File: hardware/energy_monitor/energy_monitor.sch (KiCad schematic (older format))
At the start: 134 parts, among them J1 Screw_Terminal_01x03, J2 Screw_Terminal_01x04, J3 Screw_Terminal_01x04, J4 Screw_Terminal_01x04, J5 USB_OTG, Q1 MMBT2222, Q2 MMBT2222, U1 RAC04, U2 TPS730, U3 TPS723, U4 ADS131E08, U5 AP2112, U6 CP2104, U7 ESP-WROOM-32U

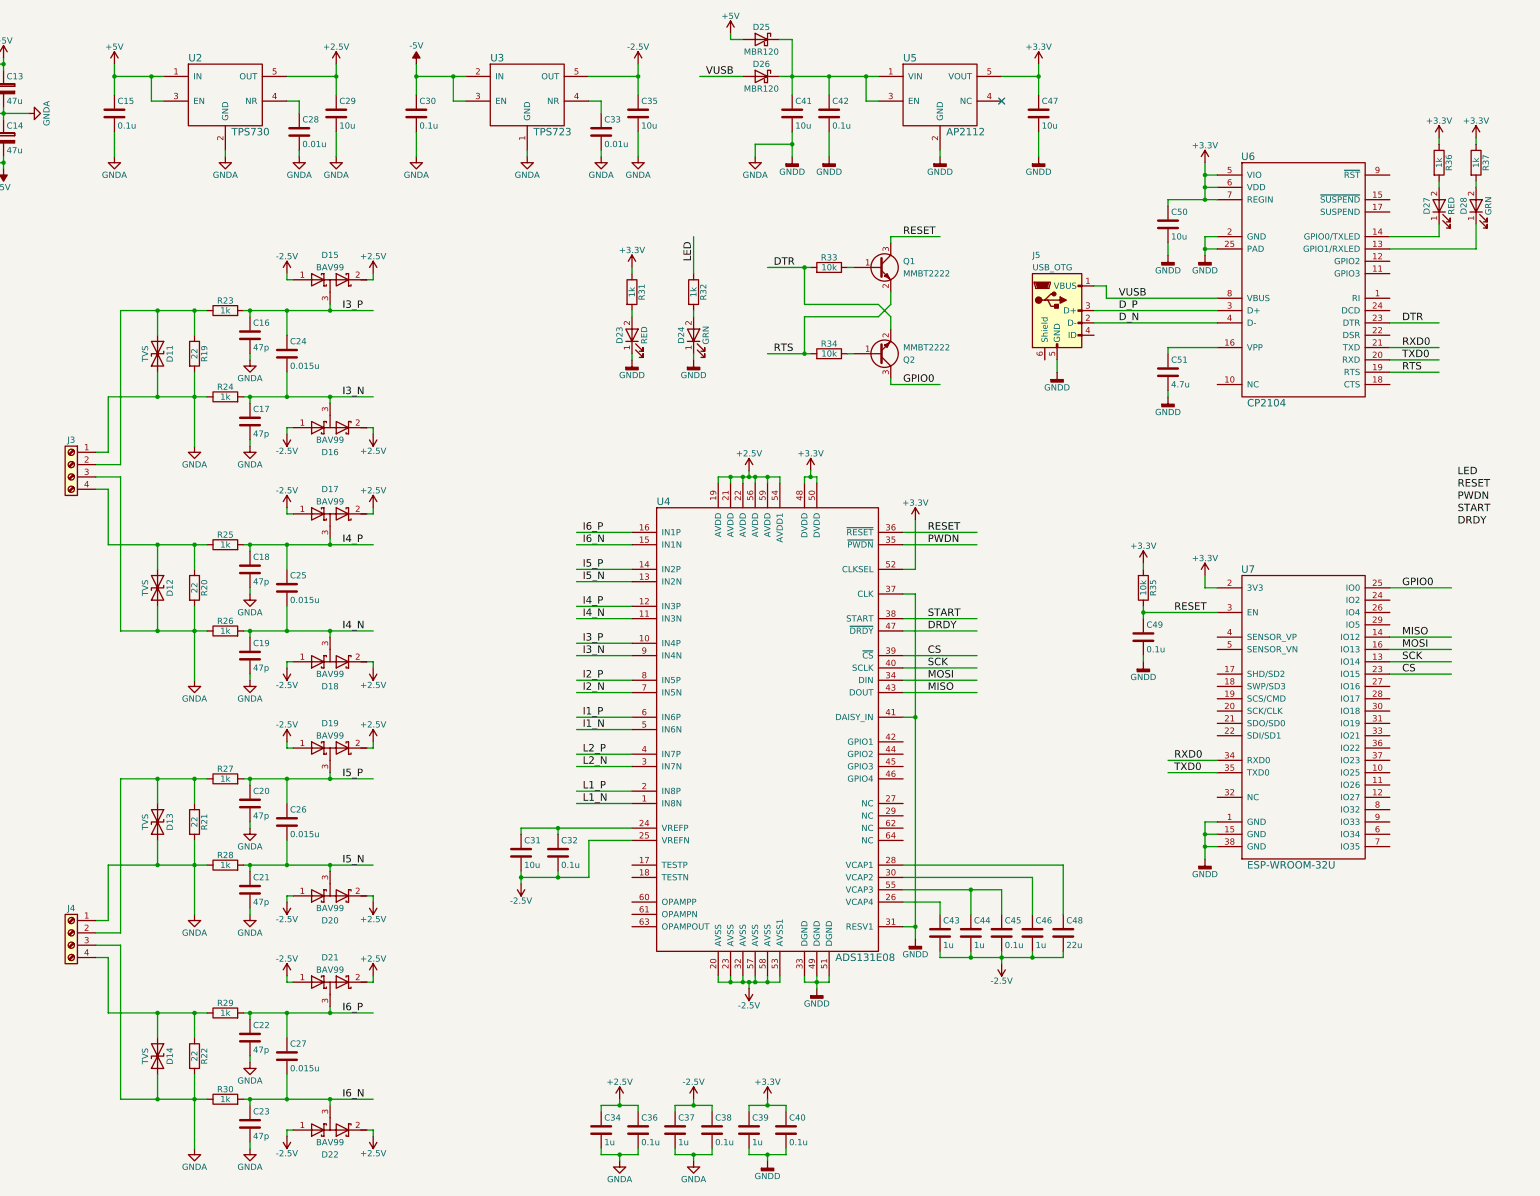
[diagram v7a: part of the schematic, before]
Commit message: Added digital isolator to USB UART circuit
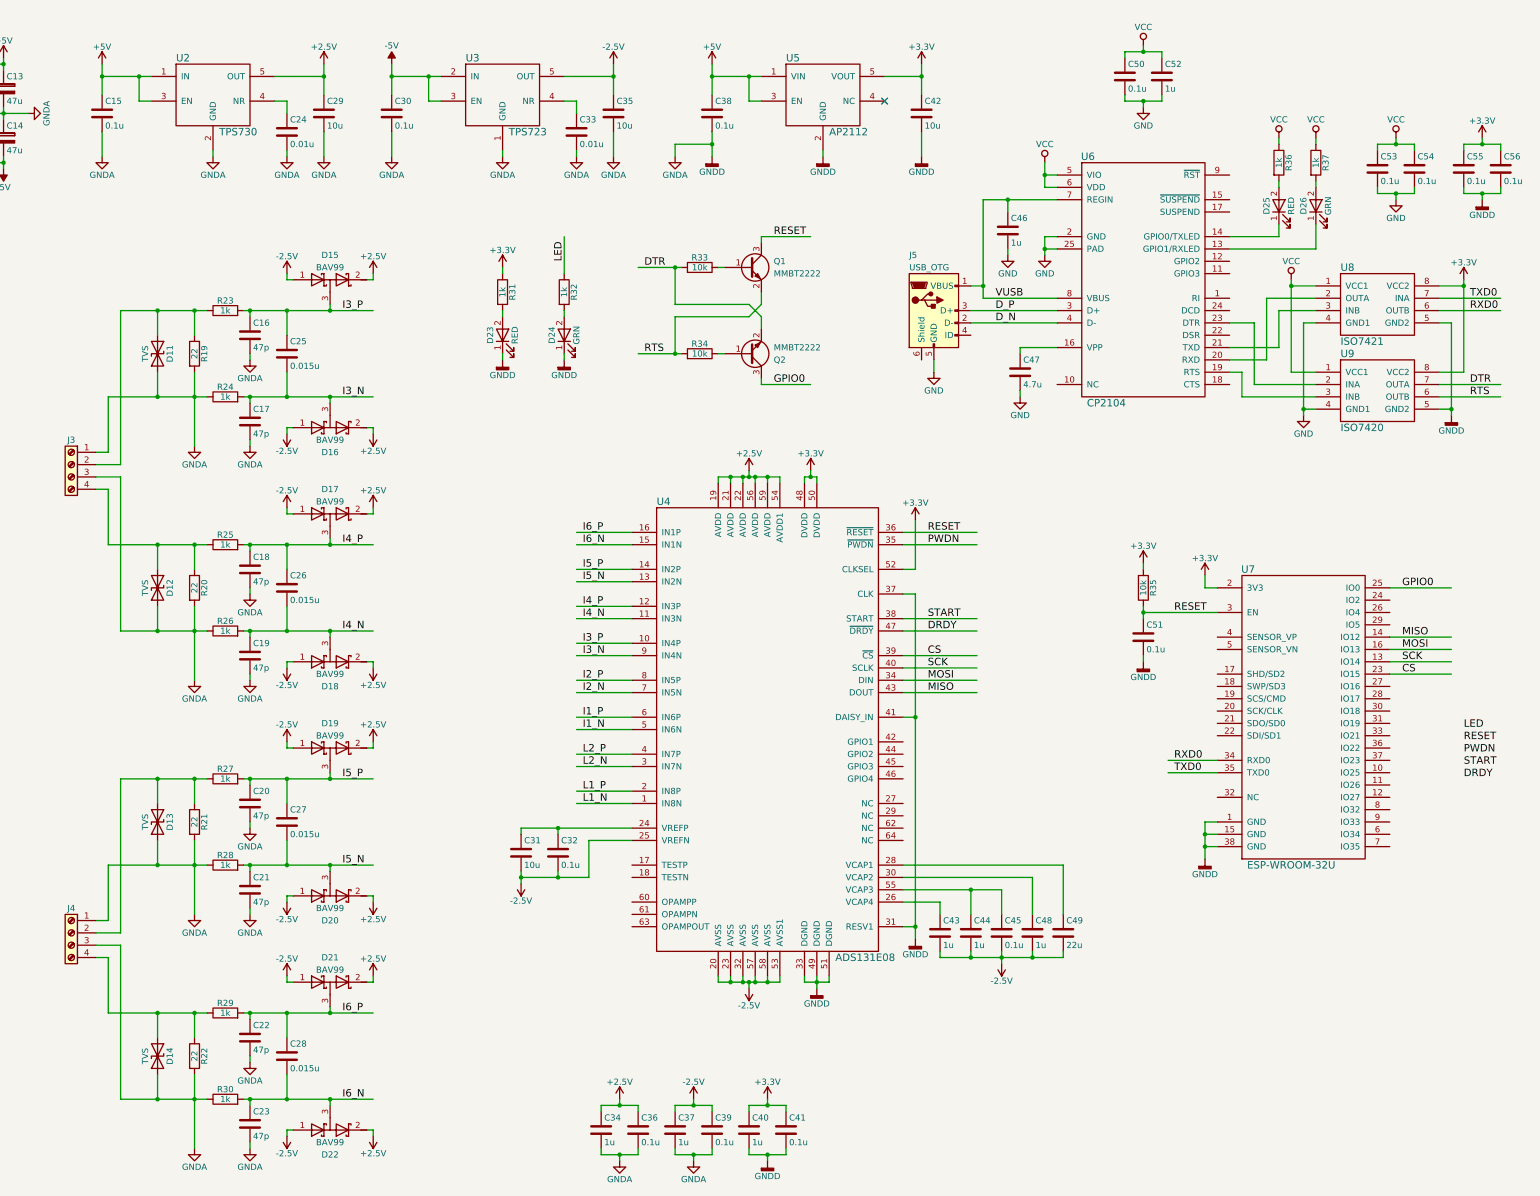
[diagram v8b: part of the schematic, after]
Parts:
- removed C41: 10u, Capacitors_SMD:C_0805, symbol C
- removed D25, D26: MBR120, footprint:SOD-123FL, symbol D_Schottky
- added C46, C52: 1u, Capacitors_SMD:C_0805, symbol C
- added C53, C54, C55, C56: 0.1u, Capacitors_SMD:C_0603, symbol C
- added U8: ISO7421, Housings_SOIC:SOIC-8_3.9x4.9mm_Pitch1.27mm, symbol ISO7421
- added U9: ISO7420, Housings_SOIC:SOIC-8_3.9x4.9mm_Pitch1.27mm, symbol ISO7420
- C50: value 10u -> 0.1u; footprint Capacitors_SMD:C_0805 -> Capacitors_SMD:C_0603; Part 490-5523-1-ND -> 490-9691-1-ND
- renumbered C28 to C24, C24 to C25, C25 to C26, C26 to C27, C27 to C28, C42 to C38, C38 to C39, C39 to C40, C40 to C41, C47 to C42, C51 to C47, C46 to C48, C48 to C49, C49 to C51, D27 to D25, D28 to D26
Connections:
- net labels added: GND, VCC
- wire segments 448 -> 490
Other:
- moved on the sheet: C15, C24, C29, C30, C33, C35, C38, C42, C47, D23, D24, D25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
